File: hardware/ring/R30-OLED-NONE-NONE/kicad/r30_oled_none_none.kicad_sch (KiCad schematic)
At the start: 0 parts

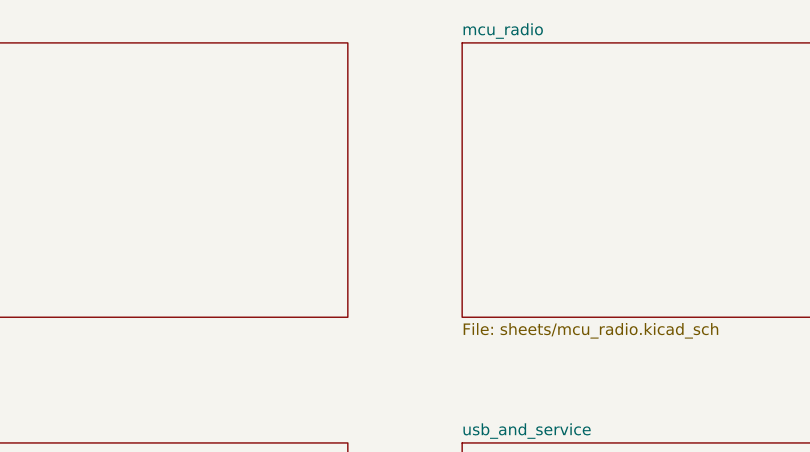
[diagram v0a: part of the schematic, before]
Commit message: feat(hardware): wire 30deg optical ring power and hub USB interfaces for accessibility pointing, ~$9 ring / ~$5-6 hub BOM
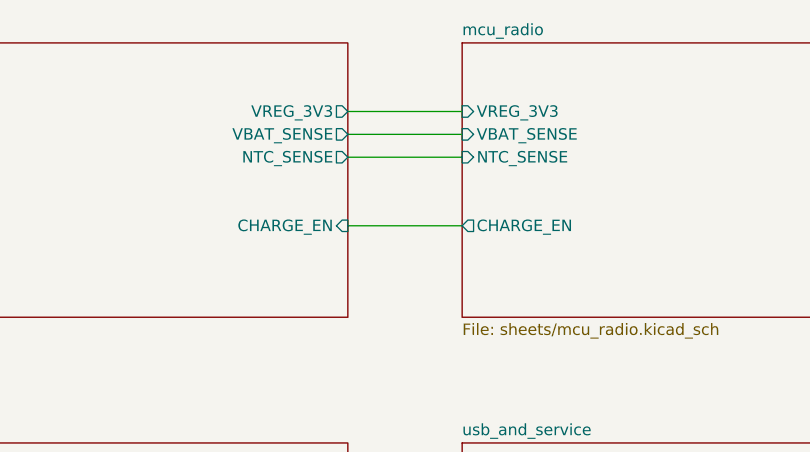
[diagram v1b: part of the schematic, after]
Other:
- sheet mcu_radio ports: added CHARGE_EN, NTC_SENSE, VBAT_SENSE, VREG_3V3; removed none
- sheet power_and_charge ports: added CHARGE_EN, NTC_SENSE, VBAT_SENSE, VREG_3V3; removed none
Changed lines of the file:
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@@
       (effects (font (size 1.27 1.27)) (justify left top))
+    )
+    (pin "VREG_3V3" output (at 101.6 33.02 0)
+      (effects (font (size 1.27 1.27)) (justify right))
+    )
+    (pin "VBAT_SENSE" output (at 101.6 35.56 0)
+      (effects (font (size 1.27 1.27)) (justify right))
+    )
+    (pin "NTC_SENSE" output (at 101.6 38.1 0)
+      (effects (font (size 1.27 1.27)) (justify right))
+    )
+    (pin "CHARGE_EN" input (at 101.6 45.72 0)
+      (effects (font (size 1.27 1.27)) (justify right))
     )
     (instances
@@
     (property "Sheet file" "sheets/mcu_radio.kicad_sch" (id 1) (at 114.3 56.5146 0)
       (effects (font (size 1.27 1.27)) (justify left top))
+    )
+    (pin "VREG_3V3" input (at 114.3 33.02 180)
+      (effects (font (size 1.27 1.27)) (justify left))
+    )
+    (pin "VBAT_SENSE" input (at 114.3 35.56 180)
+      (effects (font (size 1.27 1.27)) (justify left))
+    )
+    (pin "NTC_SENSE" input (at 114.3 38.1 180)
+      (effects (font (size 1.27 1.27)) (justify left))
+    )
+    (pin "CHARGE_EN" output (at 114.3 45.72 180)
+      (effects (font (size 1.27 1.27)) (justify left))
     )
     (instances
@@
     )
   )
+  (wire
+    (pts
+      (xy 101.6 33.02)
+      (xy 114.3 33.02)
+    )
+    (stroke (width 0) (type default) (color 0 0 0 0))
+  )
+  (wire
+    (pts
+      (xy 101.6 35.56)
+      (xy 114.3 35.56)
+    )
+    (stroke (width 0) (type default) (color 0 0 0 0))
+  )
+  (wire
+    (pts
+      (xy 101.6 38.1)
+      (xy 114.3 38.1)
+    )
+    (stroke (width 0) (type default) (color 0 0 0 0))
+  )
+  (wire
+    (pts
+      (xy 101.6 45.72)
+      (xy 114.3 45.72)
+    )
+    (stroke (width 0) (type default) (color 0 0 0 0))
+  )
   (sheet_instances

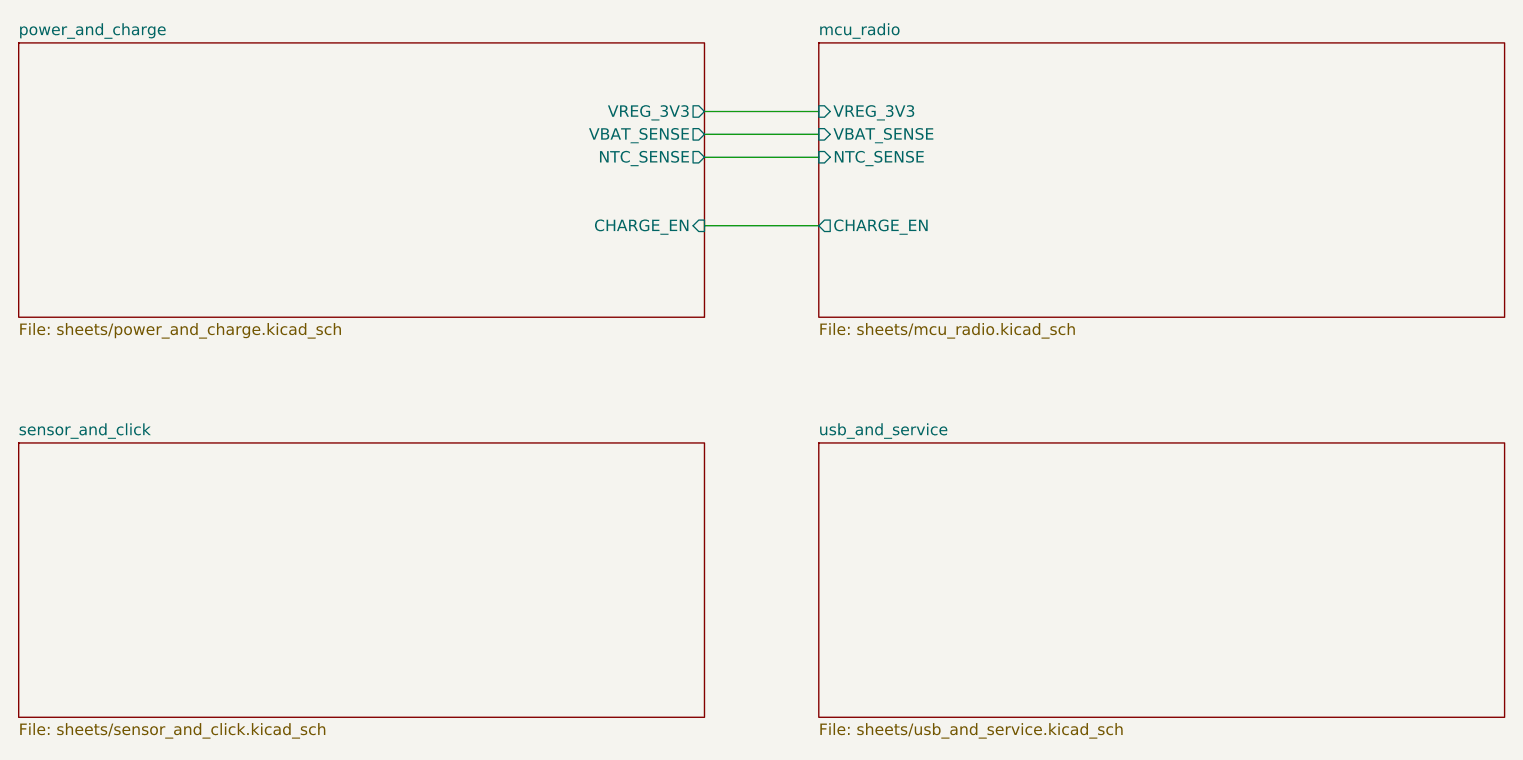
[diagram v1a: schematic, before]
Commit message: feat(hardware): wire 30deg optical ring sensor/click and usb interfaces into top sheet for accessibility pointing, ~$9 ring BOM
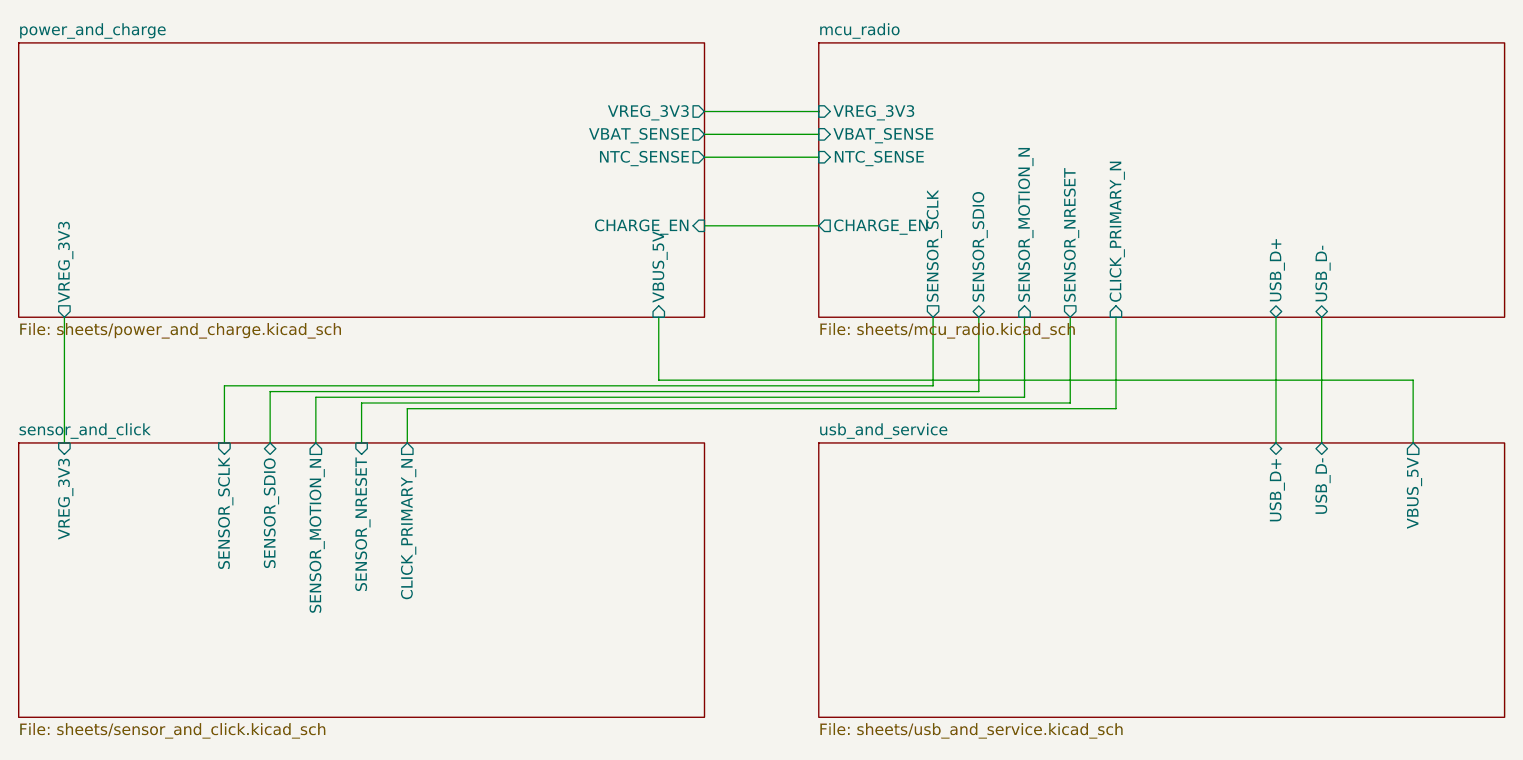
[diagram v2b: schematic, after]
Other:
- sheet mcu_radio ports: added CLICK_PRIMARY_N, SENSOR_MOTION_N, SENSOR_NRESET, SENSOR_SCLK, SENSOR_SDIO, USB_D+, USB_D-; removed none
- sheet power_and_charge ports: added VBUS_5V; removed none
- sheet sensor_and_click ports: added CLICK_PRIMARY_N, SENSOR_MOTION_N, SENSOR_NRESET, SENSOR_SCLK, SENSOR_SDIO, VREG_3V3; removed none
- sheet usb_and_service ports: added USB_D+, USB_D-, VBUS_5V; removed none
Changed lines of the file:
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@@
       (effects (font (size 1.27 1.27)) (justify right))
+    )
+    (pin "VREG_3V3" output (at 30.48 55.88 270)
+      (effects (font (size 1.27 1.27)) (justify left))
+    )
+    (pin "VBUS_5V" input (at 96.52 55.88 270)
+      (effects (font (size 1.27 1.27)) (justify left))
     )
     (instances
@@
       (effects (font (size 1.27 1.27)) (justify left))
     )
+    (pin "SENSOR_SCLK" output (at 127.0 55.88 270)
+      (effects (font (size 1.27 1.27)) (justify left))
+    )
+    (pin "SENSOR_SDIO" bidirectional (at 132.08 55.88 270)
+      (effects (font (size 1.27 1.27)) (justify left))
+    )
+    (pin "SENSOR_MOTION_N" input (at 137.16 55.88 270)
+      (effects (font (size 1.27 1.27)) (justify left))
+    )
+    (pin "SENSOR_NRESET" output (at 142.24 55.88 270)
+      (effects (font (size 1.27 1.27)) (justify left))
+    )
+    (pin "CLICK_PRIMARY_N" input (at 147.32 55.88 270)
+      (effects (font (size 1.27 1.27)) (justify left))
+    )
+    (pin "USB_D+" bidirectional (at 165.1 55.88 270)
+      (effects (font (size 1.27 1.27)) (justify left))
+    )
+    (pin "USB_D-" bidirectional (at 170.18 55.88 270)
+      (effects (font (size 1.27 1.27)) (justify left))
+    )
     (instances
       (project "r30_oled_none_none"
@@
       (effects (font (size 1.27 1.27)) (justify left top))
     )
+    (pin "VREG_3V3" input (at 30.48 69.85 90)
+      (effects (font (size 1.27 1.27)) (justify right))
+    )
+    (pin "SENSOR_SCLK" input (at 48.26 69.85 90)
+      (effects (font (size 1.27 1.27)) (justify right))
+    )
+    (pin "SENSOR_SDIO" bidirectional (at 53.34 69.85 90)
+      (effects (font (size 1.27 1.27)) (justify right))
+    )
+    (pin "SENSOR_MOTION_N" output (at 58.42 69.85 90)
+      (effects (font (size 1.27 1.27)) (justify right))
+    )
+    (pin "SENSOR_NRESET" input (at 63.5 69.85 90)
+      (effects (font (size 1.27 1.27)) (justify right))
+    )
+    (pin "CLICK_PRIMARY_N" output (at 68.58 69.85 90)
+      (effects (font (size 1.27 1.27)) (justify right))
+    )
     (instances
       (project "r30_oled_none_none"
@@
       (effects (font (size 1.27 1.27)) (justify left top))
     )
+    (pin "USB_D+" bidirectional (at 165.1 69.85 90)
+      (effects (font (size 1.27 1.27)) (justify right))
+    )
+    (pin "USB_D-" bidirectional (at 170.18 69.85 90)
+      (effects (font (size 1.27 1.27)) (justify right))
+    )
+    (pin "VBUS_5V" output (at 180.34 69.85 90)
+      (effects (font (size 1.27 1.27)) (justify right))
+    )
     (instances
       (project "r30_oled_none_none"
@@
     )
     (stroke (width 0) (type default) (color 0 0 0 0))
+  )
+  (wire
+    (pts
+      (xy 30.48 55.88)
+      (xy 30.48 69.85)
+    )
+    (stroke (width 0) (type default) (color 0 0 0 0))
+  )
+  (wire
+    (pts
+      (xy 165.1 55.88)
+      (xy 165.1 69.85)
+    )
+    (stroke (width 0) (type default) (color 0 0 0 0))
+  )
+  (wire
+    (pts
+      (xy 170.18 55.88)
+      (xy 170.18 69.85)
+    )
+    (stroke (width 0) (type default) (color 0 0 0 0))
+  )
+  (wire
+    (pts
+      (xy 48.26 69.85)
+      (xy 48.26 63.5)
+    )
+    (stroke (width 0) (type default) (color 0 0 0 0))
+  )
+  (wire
+    (pts
+      (xy 48.26 63.5)
+      (xy 127.0 63.5)
+    )
+    (stroke (width 0) (type default) (color 0 0 0 0))
+  )
+  (wire
+    (pts
+      (xy 127.0 63.5)
+      (xy 127.0 55.88)
+    )
+    (stroke (width 0) (type default) (color 0 0 0 0))
+  )
+  (wire
+    (pts
+      (xy 53.34 69.85)
+      (xy 53.34 64.14)
+    )
+    (stroke (width 0) (type default) (color 0 0 0 0))
+  )
+  (wire
+    (pts
+      (xy 53.34 64.14)
+      (xy 132.08 64.14)
+    )
+    (stroke (width 0) (type default) (color 0 0 0 0))
+  )
+  (wire
+    (pts
+      (xy 132.08 64.14)
+      (xy 132.08 55.88)
+    )
+    (stroke (width 0) (type default) (color 0 0 0 0))
+  )
+  (wire
+    (pts
+      (xy 58.42 69.85)
+      (xy 58.42 64.77)
+    )
+    (stroke (width 0) (type default) (color 0 0 0 0))
+  )
+  (wire
+    (pts
+      (xy 58.42 64.77)
+      (xy 137.16 64.77)
+    )
+    (stroke (width 0) (type default) (color 0 0 0 0))
+  )
+  (wire
+    (pts
+      (xy 137.16 64.77)
+      (xy 137.16 55.88)
+    )
+    (stroke (width 0) (type default) (color 0 0 0 0))
+  )
+  (wire
+    (pts
+      (xy 63.5 69.85)
+      (xy 63.5 65.41)
+    )
+    (stroke (width 0) (type default) (color 0 0 0 0))
+  )
+  (wire
+    (pts
+      (xy 63.5 65.41)
+      (xy 142.24 65.41)
+    )
+    (stroke (width 0) (type default) (color 0 0 0 0))
+  )
+  (wire
+    (pts
+      (xy 142.24 65.41)
+      (xy 142.24 55.88)
+    )
+    (stroke (width 0) (type default) (color 0 0 0 0))
+  )
+  (wire
+    (pts
+      (xy 68.58 69.85)
+      (xy 68.58 66.04)
+    )
+    (stroke (width 0) (type default) (color 0 0 0 0))
+  )
+  (wire
+    (pts
+      (xy 68.58 66.04)
+      (xy 147.32 66.04)
+    )
+    (stroke (width 0) (type default) (color 0 0 0 0))
+  )
+  (wire
+    (pts
+      (xy 147.32 66.04)
+      (xy 147.32 55.88)
+    )
+    (stroke (width 0) (type default) (color 0 0 0 0))
+  )
+  (wire
+    (pts
+      (xy 180.34 69.85)
+      (xy 180.34 62.87)
+    )
+    (stroke (width 0) (type default) (color 0 0 0 0))
+  )
+  (wire
+    (pts
+      (xy 180.34 62.87)
+      (xy 96.52 62.87)
+    )
+    (stroke (width 0) (type default) (color 0 0 0 0))
+  )
+  (wire
+    (pts
+      (xy 96.52 62.87)
+      (xy 96.52 55.88)
+    )
+    (stroke (width 0) (type default) (color 0 0 0 0))

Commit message: feat(hardware): lock R30 sense and schematic baseline
Design disclosure: sensing mechanism PAW3204-class optical tracking; form factor R30-OLED-NONE-NONE fingertip ring, active 30-degree ring packet; intended use BLE HID pointing for accessibility; BOM estimate ~$5.30-9.45.

Record the accepted 2N7002 charge-gate path, R7-R11 sense/status values, current KiCad red baseline, and directly linked packet truth docs.
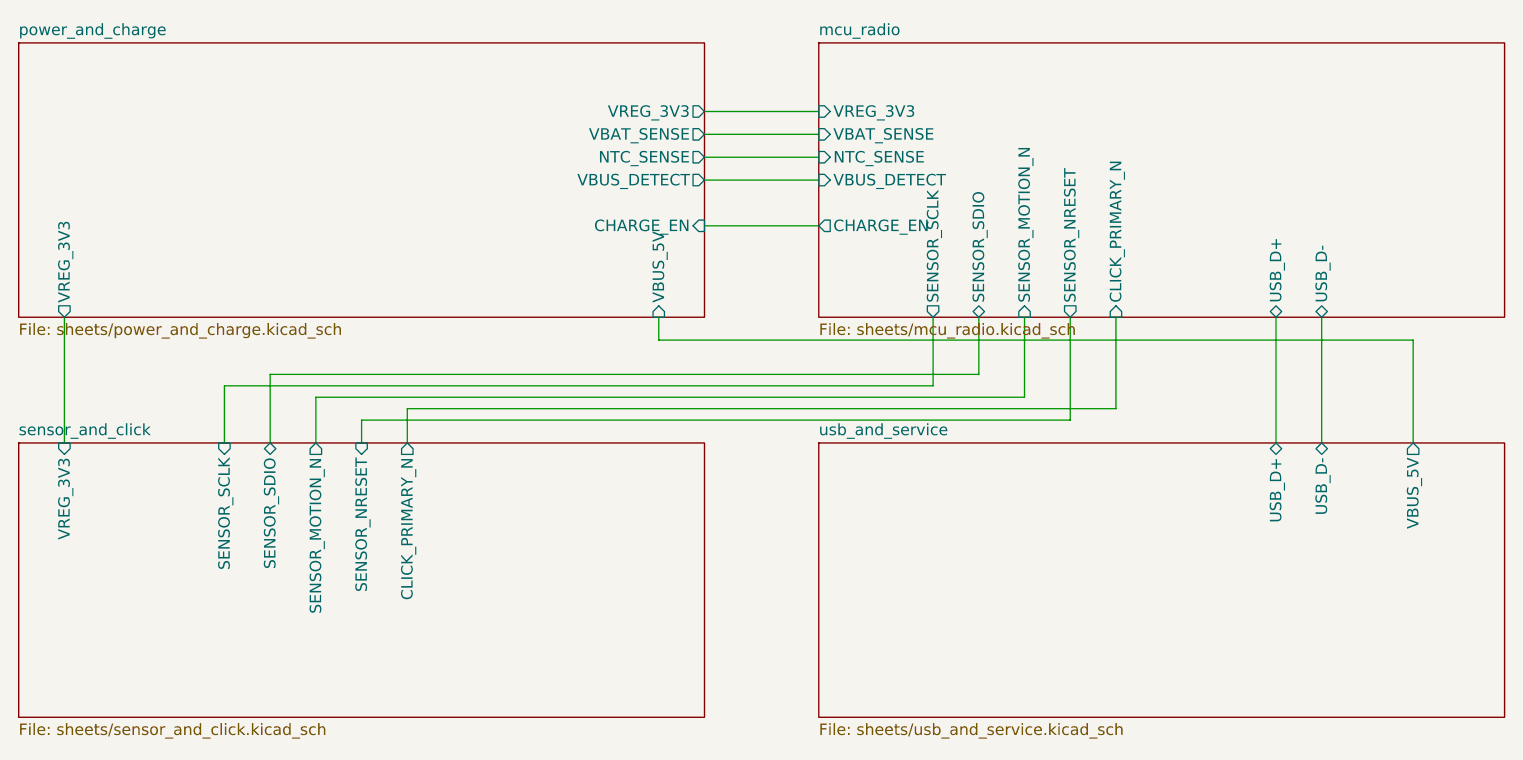
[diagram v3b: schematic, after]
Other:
- sheet mcu_radio ports: added VBUS_DETECT; removed none
- sheet power_and_charge ports: added VBUS_DETECT; removed none
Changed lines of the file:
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@@
+      (effects (font (size 1.27 1.27)) (justify right))
+    )
+    (pin "VBUS_DETECT" output (at 101.6 40.64 0)
       (effects (font (size 1.27 1.27)) (justify right))
     )
@@
       (effects (font (size 1.27 1.27)) (justify left))
     )
+    (pin "VBUS_DETECT" input (at 114.3 40.64 180)
+      (effects (font (size 1.27 1.27)) (justify left))
+    )
     (pin "CHARGE_EN" output (at 114.3 45.72 180)
       (effects (font (size 1.27 1.27)) (justify left))
@@
   (wire
     (pts
+      (xy 101.6 40.64)
+      (xy 114.3 40.64)
+    )
+    (stroke (width 0) (type default) (color 0 0 0 0))
+  )
+  (wire
+    (pts
       (xy 101.6 45.72)
       (xy 114.3 45.72)
@@
     (pts
       (xy 53.34 69.85)
-      (xy 53.34 64.14)
-    )
-    (stroke (width 0) (type default) (color 0 0 0 0))
-  )
-  (wire
-    (pts
-      (xy 53.34 64.14)
-      (xy 132.08 64.14)
-    )
-    (stroke (width 0) (type default) (color 0 0 0 0))
-  )
-  (wire
-    (pts
-      (xy 132.08 64.14)
+      (xy 53.34 62.23)
+    )
+    (stroke (width 0) (type default) (color 0 0 0 0))
+  )
+  (wire
+    (pts
+      (xy 53.34 62.23)
+      (xy 132.08 62.23)
+    )
+    (stroke (width 0) (type default) (color 0 0 0 0))
+  )
+  (wire
+    (pts
+      (xy 132.08 62.23)
       (xy 132.08 55.88)
     )
@@
     (pts
       (xy 63.5 69.85)
-      (xy 63.5 65.41)
-    )
-    (stroke (width 0) (type default) (color 0 0 0 0))
-  )
-  (wire
-    (pts
-      (xy 63.5 65.41)
-      (xy 142.24 65.41)
-    )
-    (stroke (width 0) (type default) (color 0 0 0 0))
-  )
-  (wire
-    (pts
-      (xy 142.24 65.41)
+      (xy 63.5 67.31)
+    )
+    (stroke (width 0) (type default) (color 0 0 0 0))
+  )
+  (wire
+    (pts
+      (xy 63.5 67.31)
+      (xy 142.24 67.31)
+    )
+    (stroke (width 0) (type default) (color 0 0 0 0))
+  )
+  (wire
+    (pts
+      (xy 142.24 67.31)
       (xy 142.24 55.88)
     )
@@
     (pts
       (xy 180.34 69.85)
-      (xy 180.34 62.87)
-    )
-    (stroke (width 0) (type default) (color 0 0 0 0))
-  )
-  (wire
-    (pts
-      (xy 180.34 62.87)
-      (xy 96.52 62.87)
-    )
-    (stroke (width 0) (type default) (color 0 0 0 0))
-  )
-  (wire
-    (pts
-      (xy 96.52 62.87)
+      (xy 180.34 58.42)
+    )
+    (stroke (width 0) (type default) (color 0 0 0 0))
+  )
+  (wire
+    (pts
+      (xy 180.34 58.42)
+      (xy 96.52 58.42)
+    )
+    (stroke (width 0) (type default) (color 0 0 0 0))
+  )
+  (wire
+    (pts
+      (xy 96.52 58.42)
       (xy 96.52 55.88)
     )
